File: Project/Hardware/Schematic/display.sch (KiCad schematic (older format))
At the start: 11 parts

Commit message: Byta skärm, igen igen (#11)
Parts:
- removed C? (x2): 2.2u, symbol Device:C
- removed R? (x4): 1k, symbol Device:R
- removed R?: 330, symbol Device:R
- removed R?: 33, symbol Device:R
- removed RV?: R_POT, symbol Device:R_POT
- removed U?: Oled-MCTO, PASC:MCOT064048A1V, symbol PASC:Oled-MCTO
- added R?: 330, symbol Device:R
- added U?: Nokia5110, PASC:Nokia5110, symbol PASC:Nokia5110
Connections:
- net +3V3: now also U?.1 (Vcc)
- net GND: now also U?.2 (GND)
- new net LCD_DC: U?.5 (DC)
- new net LCD_DN: U?.6 (DN)
- new net LCD_LED: R?.1
- new net LCD_RST: U?.4 (RST)
- new net LCD_SCE: U?.3 (SCE)
- new net LCD_SCK: U?.7 (SCK)
- new net LED: R?.2, U?.8 (LED)
- no-connect marks 5 -> 0

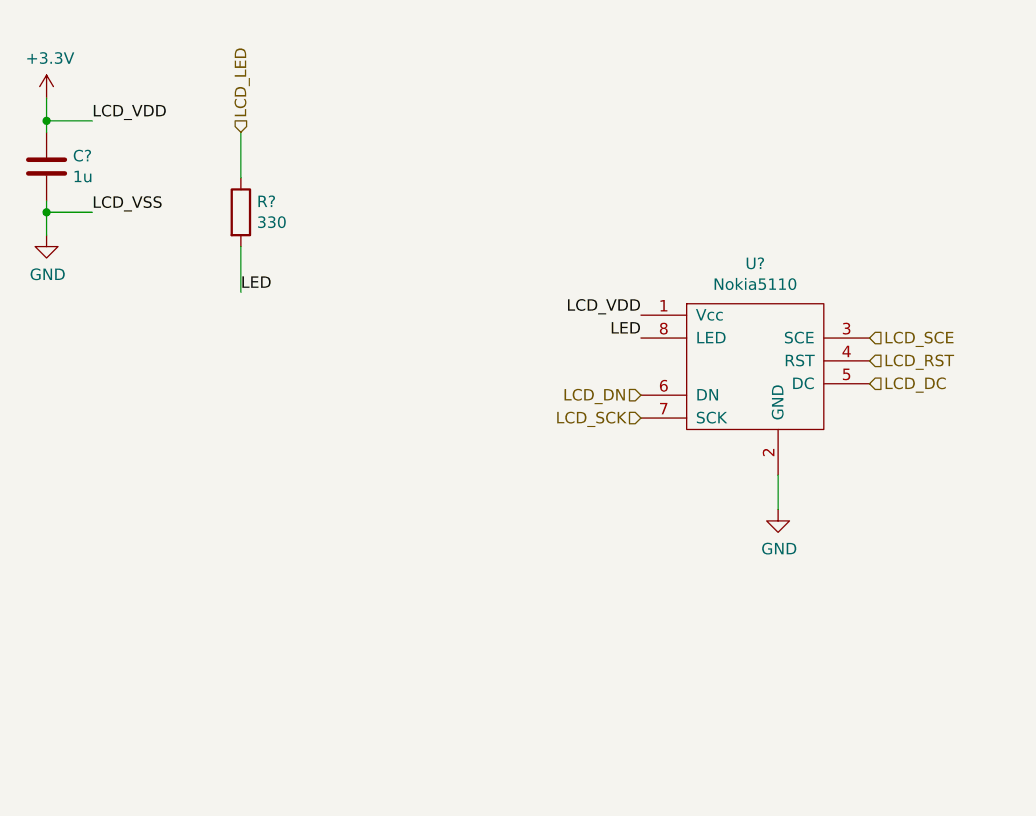
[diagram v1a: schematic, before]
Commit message: Tog bort power supply +7, lade till switch för att switcha mellan batteri och USB power. Lade till power-net symbol för oregulerad supply voltage +VIN.
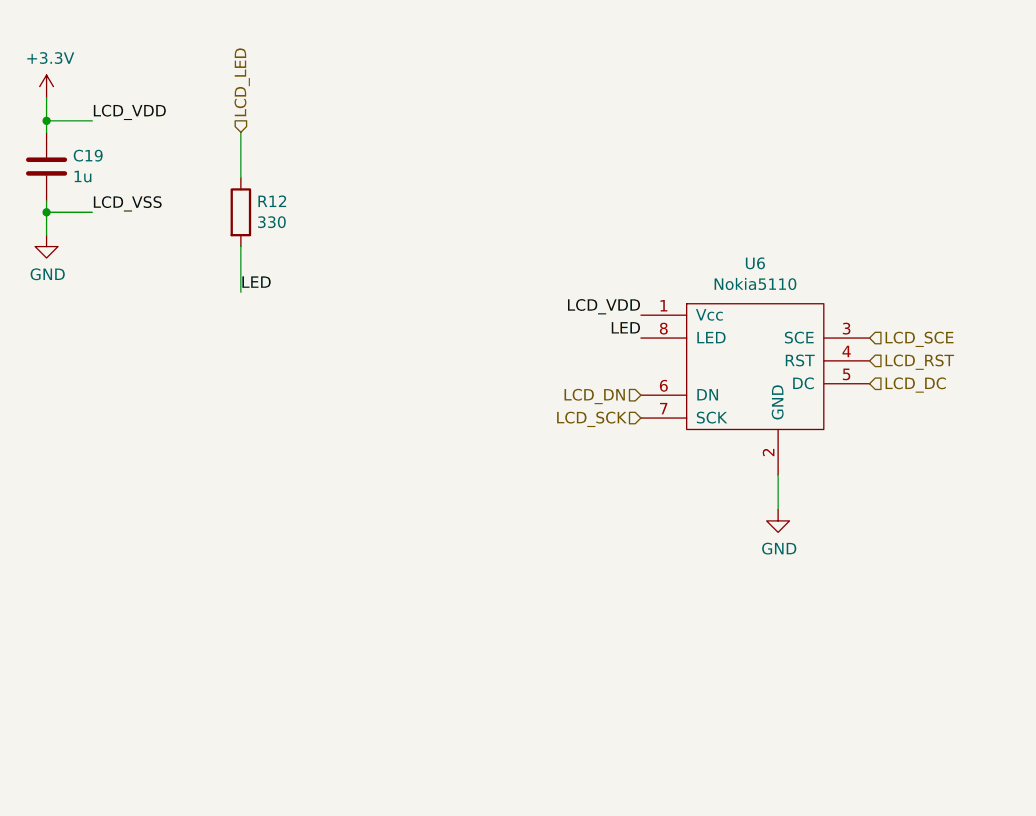
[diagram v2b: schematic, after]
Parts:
- gave numbers to parts that had none: 3
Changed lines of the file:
@@
 $EndDescr
 $Comp
-L power:GND #PWR?
+L power:GND #PWR0134
 U 1 1 5C58DE2B
 P 850 1600
-AR Path="/5C564F2E/5C58DE2B" Ref="#PWR?"  Part="1"
+AR Path="/5C564F2E/5C58DE2B" Ref="#PWR0134"  Part="1"
 AR Path="/5C5FFA20/5C58DE2B" Ref="#PWR?"  Part="1"
-F 0 "#PWR?" H 850 1350 50  0001 C CNN
+F 0 "#PWR0134" H 850 1350 50  0001 C CNN
 F 1 "GND" H 855 1427 50  0000 C CNN
 F 2 "" H 850 1600 50  0001 C CNN
@@
 $EndComp
 $Comp
-L Device:C C?
+L Device:C C19
 U 1 1 5C58DF2A
 P 850 1300
-AR Path="/5C564F2E/5C58DF2A" Ref="C?"  Part="1"
+AR Path="/5C564F2E/5C58DF2A" Ref="C19"  Part="1"
 AR Path="/5C5FFA20/5C58DF2A" Ref="C?"  Part="1"
-F 0 "C?" H 965 1346 50  0000 L CNN
+F 0 "C19" H 965 1346 50  0000 L CNN
 F 1 "1u" H 965 1255 50  0000 L CNN
 F 2 "" H 888 1150 50  0001 C CNN
@@
 LCD_VSS
 $Comp
-L power:+3.3V #PWR?
+L power:+3.3V #PWR0135
 U 1 1 5C66DBDE
 P 850 1000
-AR Path="/5C564F2E/5C66DBDE" Ref="#PWR?"  Part="1"
+AR Path="/5C564F2E/5C66DBDE" Ref="#PWR0135"  Part="1"
 AR Path="/5C5FFA20/5C66DBDE" Ref="#PWR?"  Part="1"
-F 0 "#PWR?" H 850 850 50  0001 C CNN
+F 0 "#PWR0135" H 850 850 50  0001 C CNN
 F 1 "+3.3V" H 865 1173 50  0000 C CNN
 F 2 "" H 850 1000 50  0001 C CNN
@@
 $EndComp
 $Comp
-L PASC:Nokia5110 U?
+L PASC:Nokia5110 U6
 U 1 1 5C63A382
 P 3950 2200
-F 0 "U?" H 3950 2675 50  0000 C CNN
+F 0 "U6" H 3950 2675 50  0000 C CNN
 F 1 "Nokia5110" H 3950 2584 50  0000 C CNN
 F 2 "PASC:Nokia5110" H 4000 2200 50  0001 C CNN
@@
 LCD_VDD
 $Comp
-L Device:R R?
+L Device:R R12
 U 1 1 5C63A8F8
 P 1700 1500
-F 0 "R?" H 1770 1546 50  0000 L CNN
+F 0 "R12" H 1770 1546 50  0000 L CNN
 F 1 "330" H 1770 1455 50  0000 L CNN
 F 2 "" V 1630 1500 50  0001 C CNN
@@
 LCD_LED
 $Comp
-L power:GND #PWR?
+L power:GND #PWR0136
 U 1 1 5C63AC65
 P 4050 2800
-F 0 "#PWR?" H 4050 2550 50  0001 C CNN
+F 0 "#PWR0136" H 4050 2550 50  0001 C CNN
 F 1 "GND" H 4055 2627 50  0000 C CNN
 F 2 "" H 4050 2800 50  0001 C CNN

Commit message: Intermediate...
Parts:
- C19: footprint (none) -> Capacitor_SMD:C_0805_2012Metric_Pad1.15x1.40mm_HandSolder
- R12: footprint (none) -> Resistor_SMD:R_0805_2012Metric_Pad1.15x1.40mm_HandSolder
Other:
- moved on the sheet: C19, R12, U6
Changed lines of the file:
@@
 EELAYER 26 0
 EELAYER END
-$Descr User 5906 5906
+$Descr User 5906 4724
 encoding utf-8
 Sheet 5 7
 Title ""
-Date ""
-Rev ""
-Comp ""
+Date "2019-02-12"
+Rev "1"
+Comp "PASC"
 Comment1 ""
 Comment2 ""
@@
 L power:GND #PWR0134
 U 1 1 5C58DE2B
-P 850 1600
+P 1450 1900
 AR Path="/5C564F2E/5C58DE2B" Ref="#PWR0134"  Part="1"
 AR Path="/5C5FFA20/5C58DE2B" Ref="#PWR?"  Part="1"
-F 0 "#PWR0134" H 850 1350 50  0001 C CNN
-F 1 "GND" H 855 1427 50  0000 C CNN
-F 2 "" H 850 1600 50  0001 C CNN
-F 3 "" H 850 1600 50  0001 C CNN
-	1    850  1600
+F 0 "#PWR0134" H 1450 1650 50  0001 C CNN
+F 1 "GND" H 1455 1727 50  0000 C CNN
+F 2 "" H 1450 1900 50  0001 C CNN
+F 3 "" H 1450 1900 50  0001 C CNN
+	1    1450 1900
 	1    0    0    -1
 $EndComp
@@
 L Device:C C19
 U 1 1 5C58DF2A
-P 850 1300
+P 1450 1600
 AR Path="/5C564F2E/5C58DF2A" Ref="C19"  Part="1"
 AR Path="/5C5FFA20/5C58DF2A" Ref="C?"  Part="1"
-F 0 "C19" H 965 1346 50  0000 L CNN
-F 1 "1u" H 965 1255 50  0000 L CNN
-F 2 "" H 888 1150 50  0001 C CNN
-F 3 "~" H 850 1300 50  0001 C CNN
-	1    850  1300
+F 0 "C19" H 1565 1646 50  0000 L CNN
+F 1 "1u" H 1565 1555 50  0000 L CNN
+F 2 "Capacitor_SMD:C_0805_2012Metric_Pad1.15x1.40mm_HandSolder" H 1488 1450 50  0001 C CNN
+F 3 "~" H 1450 1600 50  0001 C CNN
+	1    1450 1600
 	1    0    0    -1
 $EndComp
 Wire Wire Line
-	850  1150 850  1100
+	1450 1450 1450 1400
 Wire Wire Line
-	850  1450 850  1500
+	1450 1750 1450 1800
 Wire Wire Line
-	850  1100 1050 1100
-Connection ~ 850  1100
+	1450 1400 1650 1400
+Connection ~ 1450 1400
 Wire Wire Line
-	850  1100 850  1000
+	1450 1400 1450 1300
 Wire Wire Line
-	850  1500 1050 1500
-Connection ~ 850  1500
+	1450 1800 1650 1800
+Connection ~ 1450 1800
 Wire Wire Line
-	850  1500 850  1600
-Text Label 1050 1100 0    50   ~ 0
+	1450 1800 1450 1900
+Text Label 1650 1400 0    50   ~ 0
 LCD_VDD
-Text Label 1050 1500 0    50   ~ 0
+Text Label 1650 1800 0    50   ~ 0
 LCD_VSS
 $Comp
 L power:+3.3V #PWR0135
 U 1 1 5C66DBDE
-P 850 1000
+P 1450 1300
 AR Path="/5C564F2E/5C66DBDE" Ref="#PWR0135"  Part="1"
 AR Path="/5C5FFA20/5C66DBDE" Ref="#PWR?"  Part="1"
-F 0 "#PWR0135" H 850 850 50  0001 C CNN
-F 1 "+3.3V" H 865 1173 50  0000 C CNN
-F 2 "" H 850 1000 50  0001 C CNN
-F 3 "" H 850 1000 50  0001 C CNN
-	1    850  1000
+F 0 "#PWR0135" H 1450 1150 50  0001 C CNN
+F 1 "+3.3V" H 1465 1473 50  0000 C CNN
+F 2 "" H 1450 1300 50  0001 C CNN
+F 3 "" H 1450 1300 50  0001 C CNN
+	1    1450 1300
 	1    0    0    -1
 $EndComp
@@
 L PASC:Nokia5110 U6
 U 1 1 5C63A382
-P 3950 2200
-F 0 "U6" H 3950 2675 50  0000 C CNN
-F 1 "Nokia5110" H 3950 2584 50  0000 C CNN
-F 2 "PASC:Nokia5110" H 4000 2200 50  0001 C CNN
-F 3 "" H 4000 2200 50  0001 C CNN
-	1    3950 2200
+P 3950 1600
+F 0 "U6" H 3950 2075 50  0000 C CNN
+F 1 "Nokia5110" H 3950 1984 50  0000 C CNN
+F 2 "PASC:Nokia5110" H 4000 1600 50  0001 C CNN
+F 3 "" H 4000 1600 50  0001 C CNN
+	1    3950 1600
 	1    0    0    -1
 $EndComp
-Text Label 3450 1950 2    50   ~ 0
+Text Label 3450 1350 2    50   ~ 0
 LCD_VDD
 $Comp
 L Device:R R12
 U 1 1 5C63A8F8
-P 1700 1500
-F 0 "R12" H 1770 1546 50  0000 L CNN
-F 1 "330" H 1770 1455 50  0000 L CNN
-F 2 "" V 1630 1500 50  0001 C CNN
-F 3 "~" H 1700 1500 50  0001 C CNN
-	1    1700 1500
+P 2300 1800
+F 0 "R12" H 2370 1846 50  0000 L CNN
+F 1 "330" H 2370 1755 50  0000 L CNN
+F 2 "Resistor_SMD:R_0805_2012Metric_Pad1.15x1.40mm_HandSolder" V 2230 1800 50  0001 C CNN
+F 3 "~" H 2300 1800 50  0001 C CNN
+	1    2300 1800
 	1    0    0    -1
 $EndComp
 Wire Wire Line
-	1700 1650 1700 1850
-Text Label 1700 1850 0    50   ~ 0
+	2300 1950 2300 2150
+Text Label 2300 2150 0    50   ~ 0
 LED
-Text Label 3450 2050 2    50   ~ 0
+Text Label 3450 1450 2    50   ~ 0
 LED
 Wire Wire Line
-	1700 1350 1700 1150
-Text HLabel 1700 1150 1    50   Input ~ 0
+	2300 1650 2300 1450
+Text HLabel 2300 1450 1    50   Input ~ 0
 LCD_LED
 $Comp
 L power:GND #PWR0136
 U 1 1 5C63AC65
-P 4050 2800
-F 0 "#PWR0136" H 4050 2550 50  0001 C CNN
-F 1 "GND" H 4055 2627 50  0000 C CNN
-F 2 "" H 4050 2800 50  0001 C CNN
-F 3 "" H 4050 2800 50  0001 C CNN
-	1    4050 2800
+P 4050 2200
+F 0 "#PWR0136" H 4050 1950 50  0001 C CNN
+F 1 "GND" H 4055 2027 50  0000 C CNN
+F 2 "" H 4050 2200 50  0001 C CNN
+F 3 "" H 4050 2200 50  0001 C CNN
+	1    4050 2200
 	1    0    0    -1
 $EndComp
 Wire Wire Line
-	4050 2650 4050 2800
-Text HLabel 3450 2300 0    50   Input ~ 0
+	4050 2050 4050 2200
+Text HLabel 3450 1700 0    50   Input ~ 0
 LCD_DN
-Text HLabel 3450 2400 0    50   Input ~ 0
+Text HLabel 3450 1800 0    50   Input ~ 0
 LCD_SCK
-Text HLabel 4450 2050 2    50   Input ~ 0
+Text HLabel 4450 1450 2    50   Input ~ 0
 LCD_SCE
-Text HLabel 4450 2150 2    50   Input ~ 0
+Text HLabel 4450 1550 2    50   Input ~ 0
 LCD_RST
-Text HLabel 4450 2250 2    50   Input ~ 0
+Text HLabel 4450 1650 2    50   Input ~ 0
 LCD_DC
 $EndSCHEMATC
